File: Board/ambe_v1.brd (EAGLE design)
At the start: 100 x 80 mm, 49 parts, among them IC3 AMBE-3000LQFP-128

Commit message: Progress on routing board
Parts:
- CODEC_PORT, IO_PORT, MICRO_PORT, MICRO_PORT_1: device pinhead:1X20 -> pinhead:1X10
- moved MICRO_PORT 293.7 mm to (52.1, 45.7), turned to 90 degrees
- moved IO_PORT 288.9 mm to (29.2, 57.1)
- moved R22 271.6 mm to (47.3, 37.5), turned to 180 degrees
- moved R21 267.7 mm to (47.3, 39.7), turned to 180 degrees
- moved CODEC_PORT 264.0 mm to (47.0, 22.9), turned to 90 degrees
- moved R20 263.7 mm to (47.3, 41.9), turned to 180 degrees
- moved MICRO_PORT_1 261.0 mm to (15.2, 11.4)
- moved R19 259.7 mm to (47.3, 44.1), turned to 180 degrees
- moved R18 255.8 mm to (47.3, 46.4), turned to 180 degrees
- moved R17 251.9 mm to (47.3, 48.6), turned to 180 degrees
- moved R16 247.9 mm to (47.3, 50.8), turned to 180 degrees
- moved R15 244.0 mm to (47.3, 53.0), turned to 180 degrees
- moved LED1 231.7 mm to (43.8, 53.0), turned to 90 degrees
- moved LED2 230.3 mm to (43.8, 50.8), turned to 90 degrees
- moved LED3 229.0 mm to (43.8, 48.6), turned to 90 degrees
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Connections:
- net 1V8: now also IO_PORT.8
- net 3V3: now also IO_PORT.9
- net CONFIG10: now also MICRO_PORT_1.4; no longer MICRO_PORT_1.3
- net CONFIG11: now also MICRO_PORT_1.5; no longer MICRO_PORT_1.4
- net CONFIG12: now also MICRO_PORT_1.6; no longer MICRO_PORT_1.5
- net CONFIG13: now also MICRO_PORT_1.7; no longer MICRO_PORT_1.6
- net CONFIG14: now also MICRO_PORT_1.8; no longer MICRO_PORT_1.7
- net CONFIG15: now also MICRO_PORT_1.9; no longer MICRO_PORT_1.8
- net CONFIG8: now also MICRO_PORT_1.2; no longer MICRO_PORT_1.1
- net CONFIG9: now also MICRO_PORT_1.3; no longer MICRO_PORT_1.2
- net DSP_RESET: now also MICRO_PORT_1.1; no longer MICRO_PORT_1.9
- net GND: now also IO_PORT.7
- net RXRQST: now also MICRO_PORT.8; no longer MICRO_PORT.7
- net STAT/CONFIG1: now also SW2.10; no longer SW2.15
- net STAT/CONFIG2: now also SW2.11; no longer SW2.14
- net STAT/CONFIG3: now also SW2.12; no longer SW2.13
- net STAT/CONFIG7: now also SW2.16; no longer SW2.9
- net TXRQST: now also MICRO_PORT.7; no longer MICRO_PORT.8
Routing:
- net 3V3: track 0.00 -> 133.8 mm
- net GND: track 0.00 -> 131.4 mm, vias 0 -> 11
- net 1V8: track 0.00 -> 68.0 mm, vias 0 -> 6
- net CONFIG8: track 0.00 -> 23.6 mm
- net CONFIG0: track 0.00 -> 22.7 mm
- net CONFIG9: track 0.00 -> 21.6 mm
- net CONFIG1: track 0.00 -> 20.7 mm
- net CONFIG10: track 0.00 -> 19.6 mm
- net CONFIG2: track 0.00 -> 18.7 mm
- net DSP_RESET: track 0.00 -> 17.8 mm
- net UART0_CHAN_RX: track 0.00 -> 17.8 mm, vias 0 -> 2
- net CONFIG11: track 0.00 -> 17.6 mm
- net CONFIG3: track 0.00 -> 16.7 mm
- net CONFIG12: track 0.00 -> 15.6 mm
- net CONFIG4: track 0.00 -> 14.7 mm
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
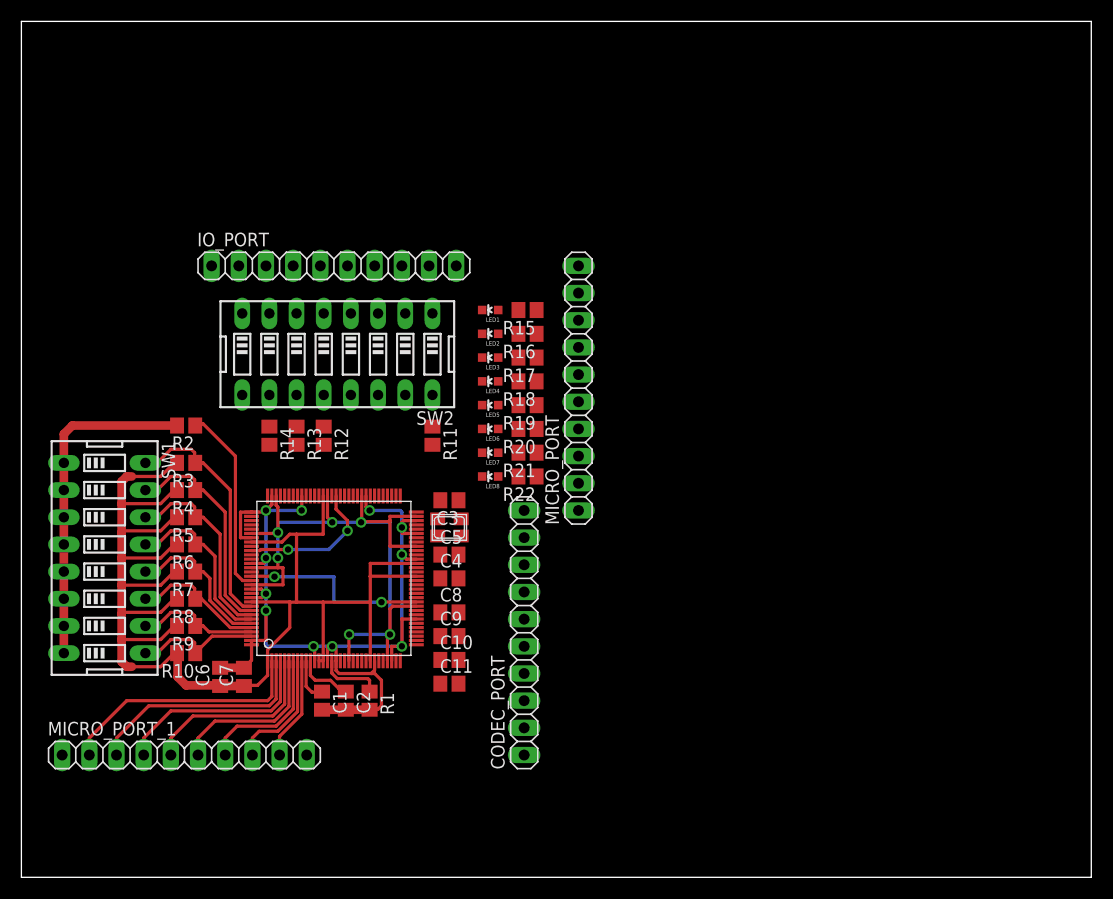
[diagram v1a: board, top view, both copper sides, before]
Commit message: Finish routing ambe board
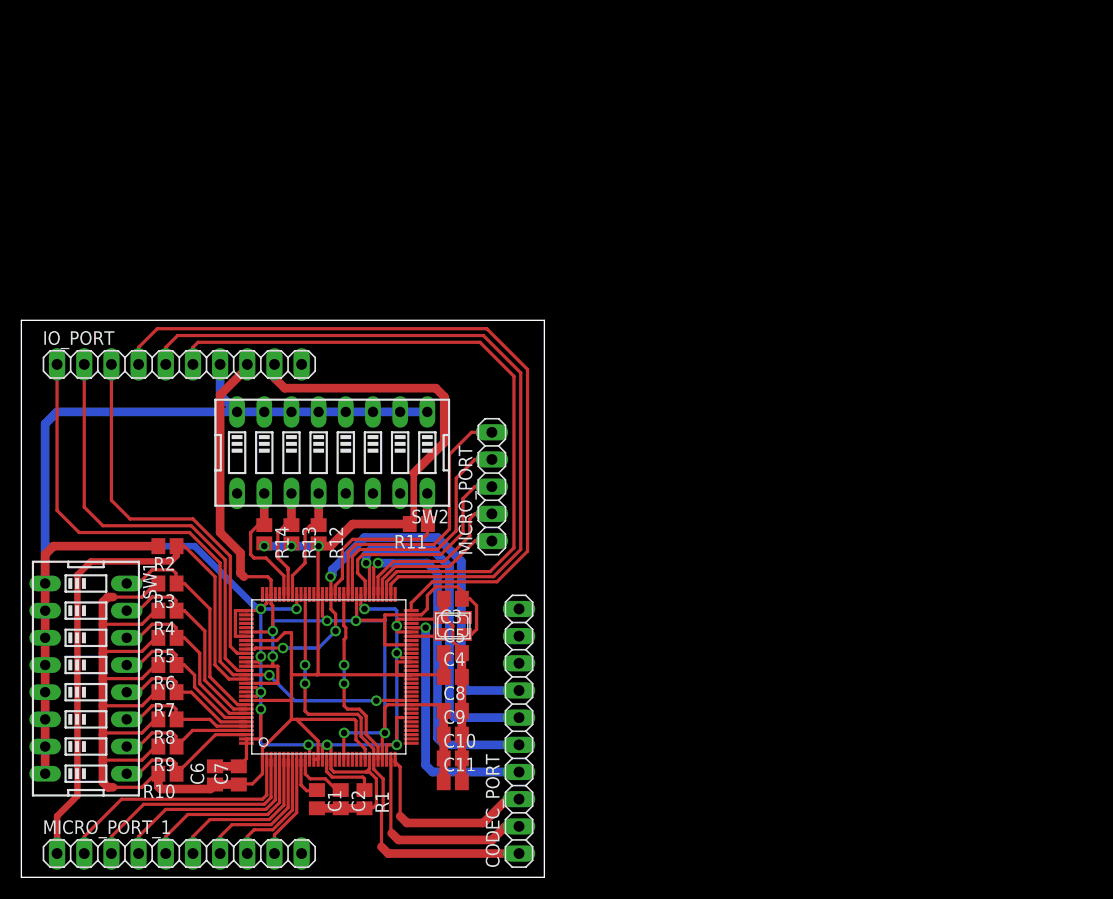
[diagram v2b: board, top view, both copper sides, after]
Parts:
- removed LED1, LED2, LED3, LED4, LED5, LED6, LED7, LED8: (no value), SparkFun-LED:LED-0603
- removed R15, R16, R17, R18, R19, R20, R21, R22: R1K, resistor:R0805
- MICRO_PORT: device pinhead:1X10 -> pinhead:1X05
- moved IO_PORT 17.1 mm to (14.8, 47.9)
- moved MICRO_PORT 12.3 mm to (44.0, 36.5)
- moved R4 11.4 mm to (13.7, 24.9)
- moved R5 11.4 mm to (13.7, 22.4)
- moved R8 11.4 mm to (13.7, 14.8)
- moved R9 11.4 mm to (13.7, 12.2)
- moved R10 11.4 mm to (13.7, 9.68)
- moved R2 11.4 mm to (13.7, 31.0)
- moved R3 11.4 mm to (13.7, 27.5)
- moved R6 11.4 mm to (13.7, 19.8)
- moved R7 11.4 mm to (13.7, 17.3)
- moved SW1 11.4 mm to (6.03, 18.6)
- moved SW2 9.22 mm to (29.1, 39.7)
- moved C1 9.22 mm to (27.6, 7.30)
- moved C2 9.22 mm to (29.8, 7.30)
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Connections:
- removed net N$1: LED1.A, R15.2
- removed net N$2: LED2.A, R16.2
- removed net N$3: LED3.A, R17.2
- removed net N$4: LED4.A, R18.2
- removed net N$5: LED5.A, R19.2
- removed net N$6: LED6.A, R20.2
- removed net N$7: LED7.A, R21.2
- removed net N$8: LED8.A, R22.2
- net 3V3: no longer R15.1, R16.1, R17.1, R18.1, R19.1, R20.1, R21.1, R22.1
- net CODEC_CLKN: now also CODEC_PORT.1; no longer CODEC_PORT.2
- net CODEC_FSN: now also CODEC_PORT.7; no longer CODEC_PORT.1
- net CODEC_RESETN: now also CODEC_PORT.4; no longer CODEC_PORT.5
- net CODEC_RX_DATA: now also CODEC_PORT.2; no longer CODEC_PORT.3
- net CODEC_TX_DATA: now also CODEC_PORT.3; no longer CODEC_PORT.4
- net HOST_DATA: now also CODEC_PORT.5; no longer CODEC_PORT.7
- net RXRDY: now also MICRO_PORT.4; no longer MICRO_PORT.2
- net RXRQST: now also MICRO_PORT.3; no longer MICRO_PORT.8
- net STAT0: no longer LED1.C
- net STAT1: no longer LED2.C
- net STAT2/UART0_RTS: now also IO_PORT.4; no longer IO_PORT.3, LED3.C
- net STAT3: no longer LED4.C
- net STAT4: no longer LED5.C
- net STAT5: no longer LED6.C
- net STAT6: no longer LED7.C
- net STAT7: no longer LED8.C
- net TXFRM: now also MICRO_PORT.5; no longer MICRO_PORT.3
- net TXRDY: now also MICRO_PORT.2; no longer MICRO_PORT.1
- net TXRQST: now also MICRO_PORT.1; no longer MICRO_PORT.7
- net UART0_CHAN_RX: now also IO_PORT.1; no longer IO_PORT.4
- net UART0_CHAN_TX: now also IO_PORT.2; no longer IO_PORT.1
- net UART0_CTS: now also IO_PORT.3; no longer IO_PORT.6
- net UART1_RX: now also IO_PORT.6; no longer IO_PORT.5
- net UART1_TX: now also IO_PORT.5; no longer IO_PORT.2
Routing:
- net GND: track 131.4 -> 231.6 mm
- net STAT2/UART0_RTS: track 0.00 -> 70.8 mm
- net UART1_TX: track 0.00 -> 67.6 mm
- net UART1_RX: track 0.00 -> 63.5 mm
- net 3V3: track 133.8 -> 191.8 mm, vias 0 -> 3
- net 1V8: track 68.0 -> 116.5 mm
- net CODEC_CLKN: track 0.00 -> 42.5 mm, vias 0 -> 2
- net UART0_CHAN_RX: track 17.8 -> 59.5 mm
- net UART0_CHAN_TX: track 0.00 -> 40.2 mm
- net DSP_RESET: track 17.8 -> 54.2 mm
- net UART0_CTS: track 0.00 -> 36.2 mm
- net CODEC_FSN: track 13.4 -> 46.3 mm, vias 2 -> 3
- net HOST_CLK: track 0.00 -> 32.8 mm, vias 0 -> 1
- net HOST_DATA: track 0.00 -> 32.3 mm, vias 0 -> 1
- net TXFRM: track 0.00 -> 26.1 mm
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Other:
- board size 100 x 80 mm -> 48.9 x 52.1 mm
